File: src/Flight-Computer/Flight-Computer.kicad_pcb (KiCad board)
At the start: 4 copper layers, 96.8 x 45.7 mm, 111 parts, among them J1 Jumper_NO, J2 Jumper_NO, P1 647676-2, P10 Micro_SD_Card, P2 1546551-2, P3 3220-20-0200-00, P4 440054-3, P5 440054-3, P6 440054-3, P7 440054-3, P8 USB, P9 1984659, Q1 QS5U17TR, Q2 QS5U17TR, Q3 QS5U17TR, Q4 QS5U17TR, Q5 QS5U17TR, Q6 QS5U17TR, U1 STM32H750VBTx, U10 TS391IYLT, U11 TS391IYLT, U12 BMM150, U2 LMS8117AMP-3.3_NOPB, U3 BMI323, U4 MAX-8C-0-10, U5 BMP390, U6 SST25VF040B-50-4I-S2AE-T, U7 RFM95W-868S2, U8 CP2102-GMR(QFN28), U9 TS391IYLT, Y1 ECS-240-18-33-JGN-TR

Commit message: finished rev 2 routing
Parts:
- moved D4 19.5 mm to (104.3, 62.0), turned to -90 degrees
- moved R27 7.48 mm to (123.1, 77.2), turned to 0 degrees
- moved R10 7.45 mm to (104.4, 91.8), turned to 180 degrees
- moved R12 7.23 mm to (102.2, 89.3), turned to 90 degrees
- moved U10 6.35 mm to (121.7, 74.2)
- moved R17 5.40 mm to (102.1, 84.6), turned to -90 degrees
- moved R11 5.29 mm to (113.5, 78.6)
- moved R34 5.21 mm to (117.7, 75.2)
- moved U11 5.21 mm to (113.8, 74.8)
- moved Q5 4.49 mm to (112.5, 70.9)
- moved BT1 4.41 mm to (106.7, 72.4)
- moved R8 4.30 mm to (106.9, 92.3), turned to 90 degrees
- moved C25 4.22 mm to (117.8, 70.9)
- moved R31 4.22 mm to (116.1, 70.7)
- moved C16 3.88 mm to (113.8, 91.2)
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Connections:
- U1 pad 18: USB_DETECT -> unconnected-(U1-Pad18)
- U1 pad 36: unconnected-(U1-Pad36) -> MAG_DRDY
- U1 pad 37: unconnected-(U1-Pad37) -> MAG_INT
- U1 pad 56: unconnected-(U1-Pad56) -> USB_DETECT
- U1 pad 81: MAG_INT -> unconnected-(U1-Pad81)
- U1 pad 82: MAG_DRDY -> unconnected-(U1-Pad82)
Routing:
- net VIN_SW: track 5.76 -> 32.6 mm
- net USB_DETECT: track 2.18 -> 28.5 mm, vias 0 -> 3
- net MAG_INT: track 1.03 -> 17.9 mm, vias 1 -> 2
- net VIN: track 223.7 -> 206.8 mm
- net MAG_DRDY: track 1.13 -> 14.0 mm, vias 1 -> 2
- net GPS_INT: track 60.2 -> 51.5 mm
- net /Navigation and Control/GPS: track 7.33 -> 15.7 mm
- net Net-(P9-Pad4): track 3.88 -> 11.6 mm
- net ~{GPS_RST}: track 57.8 -> 50.9 mm
- net 3.3V: track 88.3 -> 94.7 mm, vias 22 -> 23
- net GPS_TIM: track 68.1 -> 62.0 mm
- net ~{DROGUE_CONT}: track 34.7 -> 28.9 mm
- net ~{GPS_SBOOT}: track 33.5 -> 28.5 mm
- net /PIN_HARN: track 0.00 -> 4.73 mm
- net /PIN_SCREW: track 2.54 -> 7.27 mm
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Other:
- board size 96.8 x 45.7 mm -> 93.7 x 43.7 mm

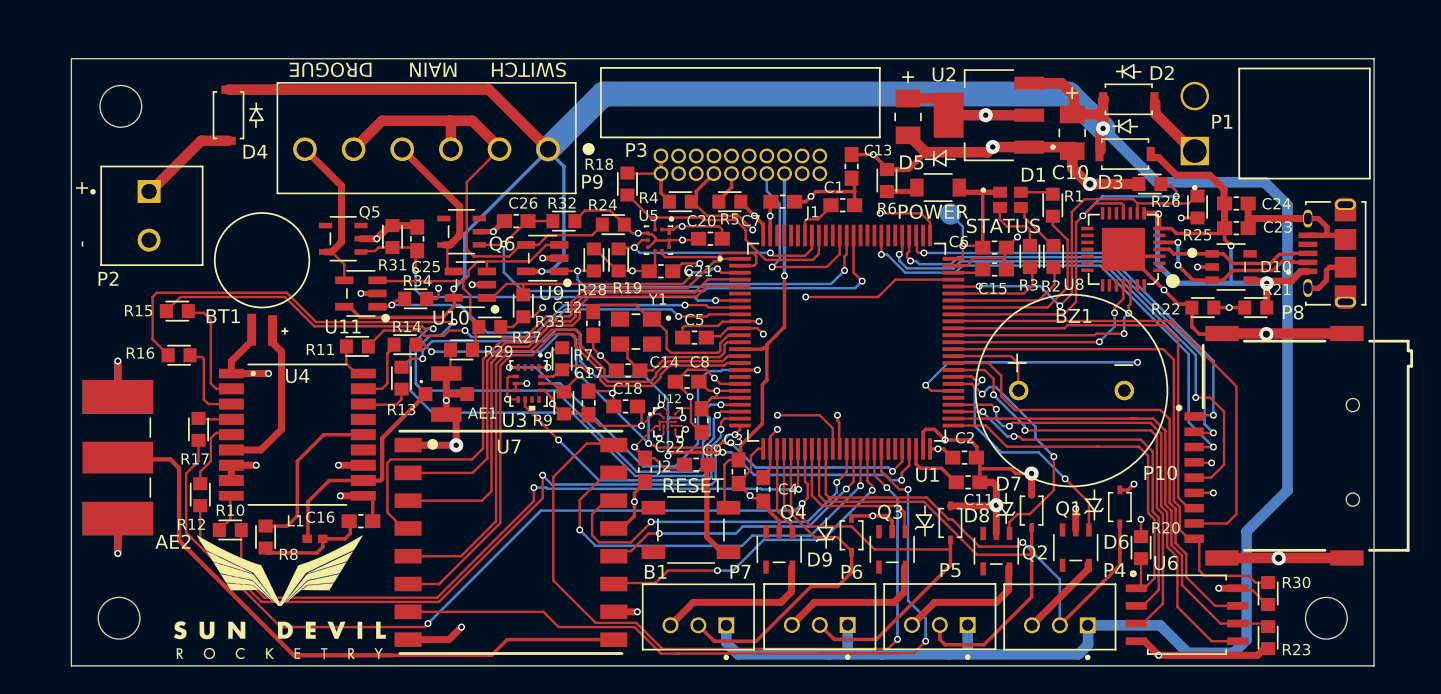
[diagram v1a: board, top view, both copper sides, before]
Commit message: resolved rev2 DRC errors
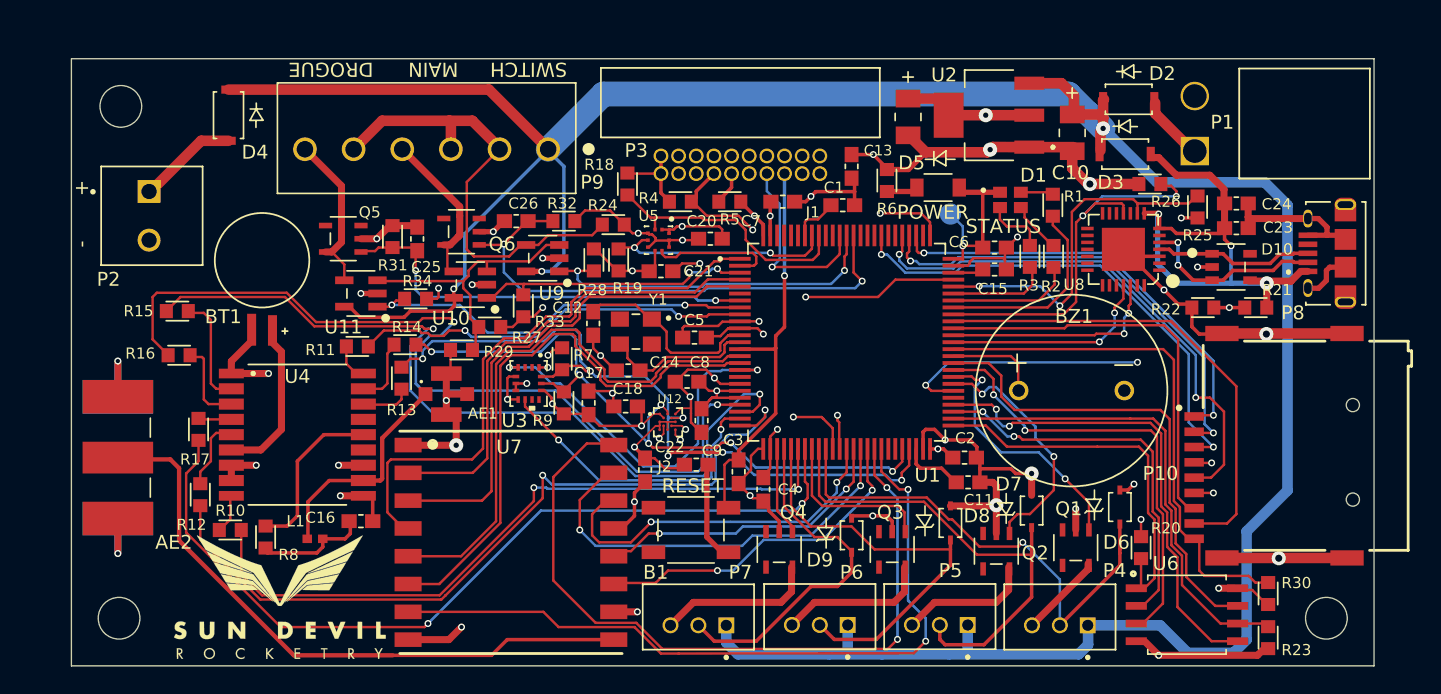
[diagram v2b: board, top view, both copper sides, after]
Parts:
- P9: value 1984659 -> CONN_1984659_PXC
- U3: value BMI323 -> BMI323_BOS
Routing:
- net GPS_INT: track 51.5 -> 56.3 mm
- net GPS_TX: track 56.1 -> 60.2 mm
- net Earth: track 217.7 -> 216.8 mm
- net NRST: track 28.3 -> 28.9 mm
- net SD_CMD: track 36.1 -> 35.6 mm
